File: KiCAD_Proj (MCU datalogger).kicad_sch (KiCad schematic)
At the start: 25 parts, among them U1 24LC1025-I_SM, U2 DS1337S_, U3 24LC1025-I_SM, U4 ATMEGA328P-AU, Y1 32.768 KHz, Y2 16MHz

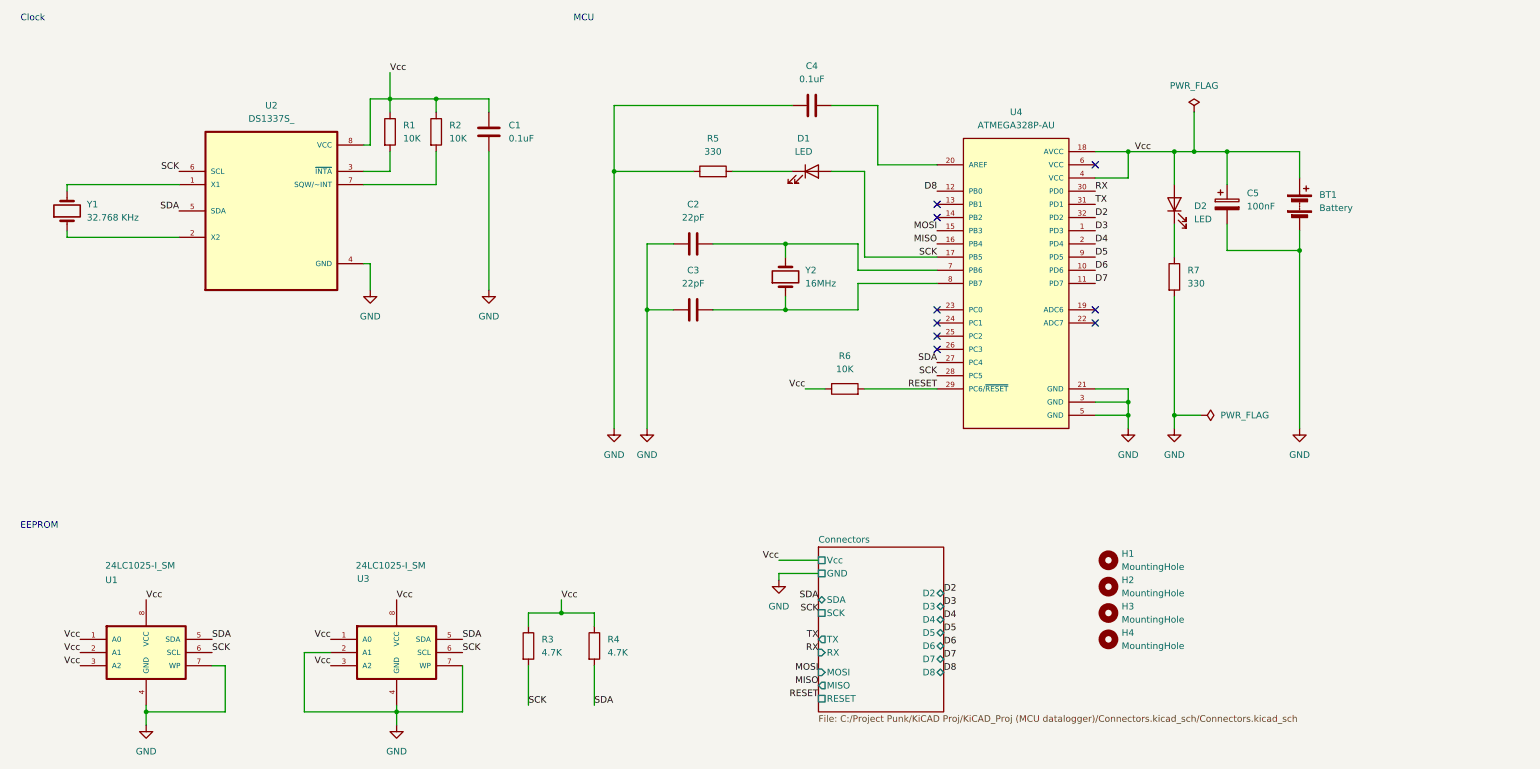
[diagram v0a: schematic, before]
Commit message: Added required symbols to schematic sheets and connectors
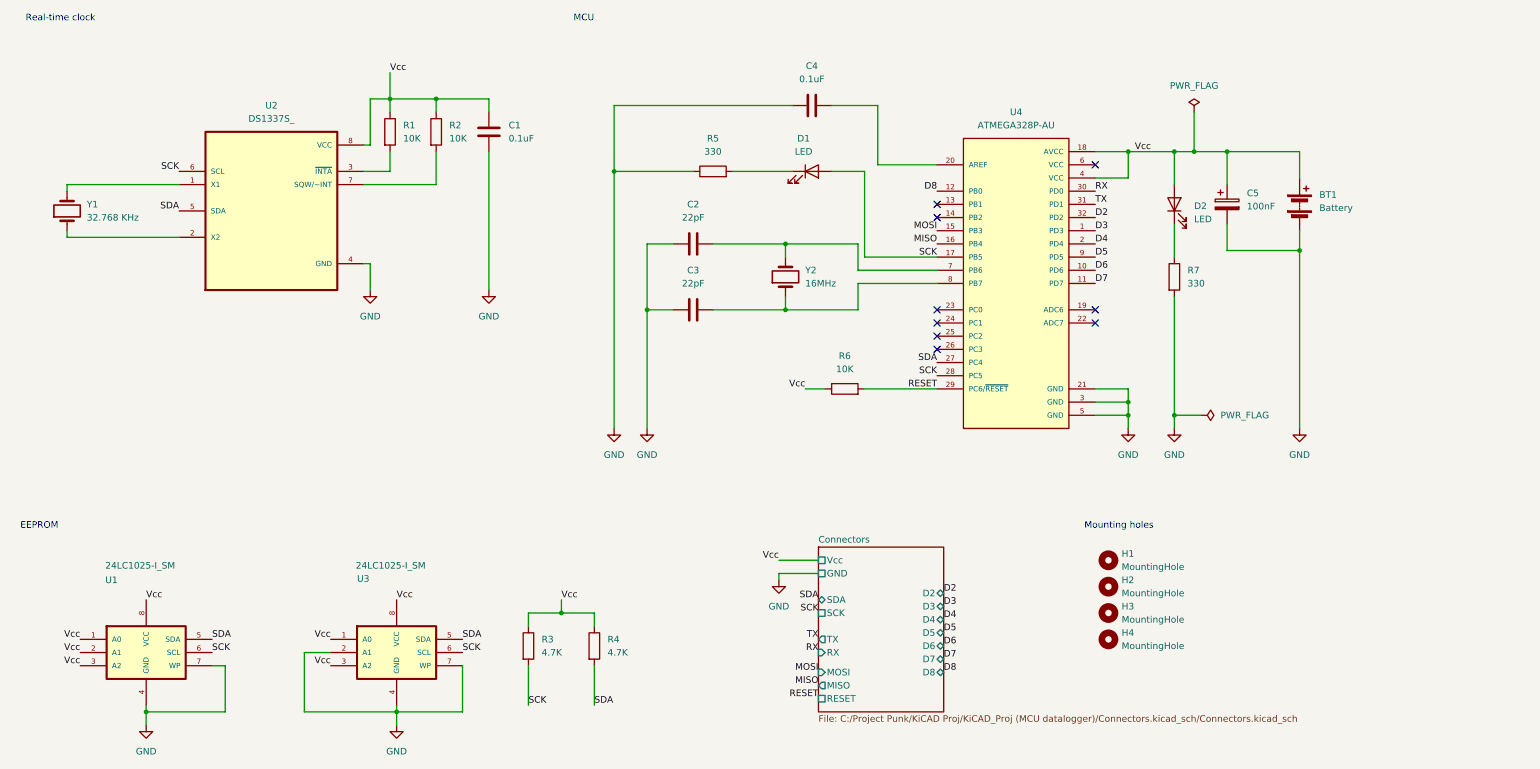
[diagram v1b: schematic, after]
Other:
- note added: "Mounting holes"
- note added: "Real-time clock"
- note removed: "Clock"
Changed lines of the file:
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@@
 		)
 	)
-	(text "Clock"
+	(text "Real-time clock"
 		(exclude_from_sim no)
-		(at 21.336 18.796 0)
+		(at 26.67 18.796 0)
+		(effects
+			(font
+				(size 1.27 1.27)
+			)
+		)
+	)
+	(text "Mounting holes"
+		(exclude_from_sim no)
+		(at 230.632 116.586 0)
 		(effects
 			(font
@@
 			)
 			(stroke
+				(width 0)
+				(type dash)
+			)
+			(fill
+				(type none)
+			)
+		)
+	)
+	(rule_area
+		(polyline
+			(pts
+				(xy 223.52 118.11) (xy 248.92 118.11) (xy 248.92 144.78) (xy 223.52 144.78)
+			)
+			(stroke

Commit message: Routing sans GND Vcc Complete.
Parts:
- C1, C2, C3, C4, C5: footprint (none) -> Capacitor_SMD:C_0805_2012Metric
- D1, D2: footprint (none) -> LED_SMD:LED_0805_2012Metric
- H1, H2, H3, H4: footprint (none) -> MountingHole:MountingHole_2.1mm
- R1, R2, R3, R4, R5, R6, R7: footprint (none) -> Resistor_SMD:R_0805_2012Metric
- Y1, Y2: footprint (none) -> Crystal:Crystal_SMD_5032-2Pin_5.0x3.2mm_HandSoldering
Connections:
- net Vcc: no longer BT1.1 (+), C5.1, D2.2 (A), U4.18 (AVCC), U4.4 (VCC)
- new net: BT1.1 (+), C5.1, D2.2 (A), U4.18 (AVCC), U4.4 (VCC)
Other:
- moved on the sheet: H1, H2, H3, H4
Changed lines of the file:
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@@
 	(text "Mounting holes"
 		(exclude_from_sim no)
-		(at 230.632 116.586 0)
+		(at 228.092 119.126 0)
 		(effects
 			(font
@@
 		)
 	)
-	(label "Vcc"
-		(at 233.68 44.45 0)
-		(effects
-			(font
-				(size 1.27 1.27)
-			)
-			(justify left bottom)
-		)
-	)
 	(label "SCK"
 		(at 116.84 151.13 0)
@@
 		(polyline
 			(pts
-				(xy 223.52 118.11) (xy 248.92 118.11) (xy 248.92 144.78) (xy 223.52 144.78)
+				(xy 220.98 120.65) (xy 246.38 120.65) (xy 246.38 147.32) (xy 220.98 147.32)
 			)
 			(stroke
@@
 	(symbol
 		(lib_id "Mechanical:MountingHole")
-		(at 228.6 133.35 0)
+		(at 226.06 135.89 0)
 		(unit 1)
 		(exclude_from_sim no)
@@
 		(fields_autoplaced yes)
 		(property "Reference" "H3"
-			(at 231.14 132.0799 0)
+			(at 228.6 134.6199 0)
 			(effects
 				(font
@@
 		)
 		(property "Value" "MountingHole"
-			(at 231.14 134.6199 0)
+			(at 228.6 137.1599 0)
 			(effects
 				(font
@@
 			)
 		)
-		(property "Footprint" ""
-			(at 228.6 133.35 0)
+		(property "Footprint" "MountingHole:MountingHole_2.1mm"
+			(at 226.06 135.89 0)
 			(effects
 				(font
@@
 		)
 		(property "Datasheet" "~"
-			(at 228.6 133.35 0)
+			(at 226.06 135.89 0)
 			(effects
 				(font
@@
 		)
 		(property "Description" "Mounting Hole without connection"
-			(at 228.6 133.35 0)
+			(at 226.06 135.89 0)
 			(effects
 				(font
@@
 	(symbol
 		(lib_id "Mechanical:MountingHole")
-		(at 228.6 138.43 0)
+		(at 226.06 140.97 0)
 		(unit 1)
 		(exclude_from_sim no)
@@
 		(fields_autoplaced yes)
 		(property "Reference" "H4"
-			(at 231.14 137.1599 0)
+			(at 228.6 139.6999 0)
 			(effects
 				(font
@@
 		)
 		(property "Value" "MountingHole"
-			(at 231.14 139.6999 0)
+			(at 228.6 142.2399 0)
 			(effects
 				(font
@@
 			)
 		)
-		(property "Footprint" ""
-			(at 228.6 138.43 0)
+		(property "Footprint" "MountingHole:MountingHole_2.1mm"
+			(at 226.06 140.97 0)
 			(effects
 				(font
@@
 		)
 		(property "Datasheet" "~"
-			(at 228.6 138.43 0)
+			(at 226.06 140.97 0)
 			(effects
 				(font
@@
 		)
 		(property "Description" "Mounting Hole without connection"
-			(at 228.6 138.43 0)
+			(at 226.06 140.97 0)
 			(effects
 				(font
@@
 			)
 		)
-		(property "Footprint" ""
+		(property "Footprint" "Capacitor_SMD:C_0805_2012Metric"
 			(at 152.4 73.9648 0)
 			(effects
@@
 			)
 		)
-		(property "Footprint" ""
+		(property "Footprint" "Capacitor_SMD:C_0805_2012Metric"
 			(at 175.26 34.5948 0)
 			(effects
@@
 	(symbol
 		(lib_id "Mechanical:MountingHole")
-		(at 228.6 128.27 0)
+		(at 226.06 130.81 0)
 		(unit 1)
 		(exclude_from_sim no)
@@
 		(fields_autoplaced yes)
 		(property "Reference" "H2"
-			(at 231.14 126.9999 0)
+			(at 228.6 129.5399 0)
 			(effects
 				(font
@@
 		)
 		(property "Value" "MountingHole"
-			(at 231.14 129.5399 0)
+			(at 228.6 132.0799 0)
 			(effects
 				(font
@@
 			)
 		)
-		(property "Footprint" ""
-			(at 228.6 128.27 0)
+		(property "Footprint" "MountingHole:MountingHole_2.1mm"
+			(at 226.06 130.81 0)
 			(effects
 				(font
@@
 		)
 		(property "Datasheet" "~"
-			(at 228.6 128.27 0)
+			(at 226.06 130.81 0)
 			(effects
 				(font
@@
 		)
 		(property "Description" "Mounting Hole without connection"
-			(at 228.6 128.27 0)
+			(at 226.06 130.81 0)
 			(effects
 				(font
@@
 	(symbol
 		(lib_id "Mechanical:MountingHole")
-		(at 228.6 123.19 0)
+		(at 226.06 125.73 0)
 		(unit 1)
 		(exclude_from_sim no)
@@
 		(fields_autoplaced yes)
 		(property "Reference" "H1"
-			(at 231.14 121.9199 0)
+			(at 228.6 124.4599 0)
 			(effects
 				(font
@@
 		)
 		(property "Value" "MountingHole"
-			(at 231.14 124.4599 0)
+			(at 228.6 126.9999 0)
 			(effects
 				(font
@@
 			)
 		)
-		(property "Footprint" ""
-			(at 228.6 123.19 0)
+		(property "Footprint" "MountingHole:MountingHole_2.1mm"
+			(at 226.06 125.73 0)
 			(effects
 				(font
@@
 		)
 		(property "Datasheet" "~"
-			(at 228.6 123.19 0)
+			(at 226.06 125.73 0)
 			(effects
 				(font
@@
 		)
 		(property "Description" "Mounting Hole without connection"
-			(at 228.6 123.19 0)
+			(at 226.06 125.73 0)
 			(effects
 				(font
@@
 			)
 		)
-		(property "Footprint" ""
+		(property "Footprint" "Resistor_SMD:R_0805_2012Metric"
 			(at 97.282 40.64 90)
 			(effects
@@
 			)
 		)
-		(property "Footprint" ""
+		(property "Footprint" "Crystal:Crystal_SMD_5032-2Pin_5.0x3.2mm_HandSoldering"
 			(at 27.94 55.88 0)
 			(effects
@@
 			)
 		)
-		(property "Footprint" ""
+		(property "Footprint" "Crystal:Crystal_SMD_5032-2Pin_5.0x3.2mm_HandSoldering"
 			(at 166.37 68.58 0)
 			(effects
@@
 			)
 		)
-		(property "Footprint" ""
+		(property "Footprint" "Resistor_SMD:R_0805_2012Metric"
 			(at 88.392 40.64 90)
 			(effects
@@
 			)
 		)
-		(property "Footprint" ""
+		(property "Footprint" "Capacitor_SMD:C_0805_2012Metric"
 			(at 110.1852 44.45 0)
 			(effects
@@
 			)
 		)
-		(property "Footprint" ""
+		(property "Footprint" "Capacitor_SMD:C_0805_2012Metric"
 			(at 252.4252 58.42 0)
 			(effects
@@
 			)
 		)
-		(property "Footprint" ""
+		(property "Footprint" "Resistor_SMD:R_0805_2012Metric"
 			(at 239.522 68.58 90)
 			(effects
@@
 			)
 		)
-		(property "Footprint" ""
+		(property "Footprint" "Resistor_SMD:R_0805_2012Metric"
 			(at 177.8 91.948 90)
 			(effects
@@
 			)
 		)
-		(property "Footprint" ""
+		(property "Footprint" "Resistor_SMD:R_0805_2012Metric"
 			(at 152.4 50.038 90)
 			(effects
@@
 			)
 		)
-		(property "Footprint" ""
+		(property "Footprint" "Resistor_SMD:R_0805_2012Metric"
 			(at 115.062 139.7 90)
 			(effects
@@
 			)
 		)
-		(property "Footprint" ""
+		(property "Footprint" "LED_SMD:LED_0805_2012Metric"
 			(at 171.45 48.26 0)
 			(effects
@@
 			)
 		)
-		(property "Footprint" ""
+		(property "Footprint" "LED_SMD:LED_0805_2012Metric"
 			(at 241.3 54.61 0)
 			(effects
@@
 			)
 		)
-		(property "Footprint" ""
+		(property "Footprint" "Resistor_SMD:R_0805_2012Metric"
 			(at 127.762 139.7 90)
 			(effects
@@
 			)
 		)
-		(property "Footprint" ""
+		(property "Footprint" "Capacitor_SMD:C_0805_2012Metric"
 			(at 152.4 61.2648 0)
 			(effects

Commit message: Fixed outstanding issues.
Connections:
- net Vcc: now also BT1.1 (+), C5.1, D2.2 (A), U4.18 (AVCC), U4.4 (VCC)
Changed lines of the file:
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@@
+		)
+	)
+	(label "Vcc"
+		(at 257.81 44.45 0)
+		(effects
+			(font
+				(size 1.27 1.27)
+			)
+			(justify left bottom)
 		)
 	)

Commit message: Finished the schematic.
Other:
- sheet Connectors: file C:/Project Punk/KiCAD Proj/KiCAD_Proj (MCU datalogger)/Connectors.kicad_sch/Connectors.kicad_sch -> C:/Project Punk/KiCAD Proj/KiCAD_Proj (MCU datalogger [4 layer])/Connectors.kicad_sch/Connectors.kicad_sch
- company: (none) -> LAUDE, RUSELLE RAE D.
- title: (none) -> MCU Datalogger
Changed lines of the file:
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@@
 	(generator_version "9.0")
 	(paper "A4")
+	(title_block
+		(title "MCU Datalogger")
+		(date "9/16/2025")
+		(company "LAUDE, RUSELLE RAE D.")
+		(comment 1 "BSECE - 1C")
+		(comment 2 "ELECTRONICS ENGINEERING DEPARTMENT")
+		(comment 3 "ELECTRONICS ENGINEERING")
+		(comment 4 "TECHNOLOGICAL UNIVERSITY OF THE PHILIPPINES")
+	)
 	(text "EEPROM"
 		(exclude_from_sim no)
@@
 	(wire
 		(pts
-			(xy 172.72 125.73) (xy 165.1 125.73)
-		)
-		(stroke
-			(width 0)
-			(type default)
-		)
-	)
-	(wire
-		(pts
 			(xy 91.44 152.4) (xy 104.14 152.4)
 		)
@@
 	(wire
 		(pts
+			(xy 165.1 123.19) (xy 172.72 123.19)
+		)
+		(stroke
+			(width 0)
+			(type default)
+		)
+	)
+	(wire
+		(pts
 			(xy 85.09 48.26) (xy 90.17 48.26)
 		)
@@
 	(wire
 		(pts
-			(xy 27.94 60.96) (xy 49.53 60.96)
+			(xy 172.72 125.73) (xy 165.1 125.73)
 		)
 		(stroke
@@
 	(wire
 		(pts
-			(xy 55.88 143.51) (xy 58.42 143.51)
+			(xy 27.94 60.96) (xy 49.53 60.96)
 		)
 		(stroke
@@
 	(wire
 		(pts
-			(xy 86.36 66.04) (xy 86.36 71.12)
+			(xy 55.88 143.51) (xy 58.42 143.51)
 		)
 		(stroke
@@
 	(wire
 		(pts
-			(xy 165.1 125.73) (xy 165.1 127)
+			(xy 86.36 66.04) (xy 86.36 71.12)
 		)
 		(stroke
@@
 	(wire
 		(pts
+			(xy 165.1 125.73) (xy 165.1 127)
+		)
+		(stroke
+			(width 0)
+			(type default)
+		)
+	)
+	(wire
+		(pts
 			(xy 129.54 135.89) (xy 129.54 133.35)
 		)
@@
 	(wire
 		(pts
-			(xy 165.1 123.19) (xy 172.72 123.19)
-		)
-		(stroke
-			(width 0)
-			(type default)
-		)
-	)
-	(wire
-		(pts
 			(xy 241.3 95.25) (xy 241.3 97.79)
 		)
@@
 			)
 		)
-		(property "Sheetfile" "C:/Project Punk/KiCAD Proj/KiCAD_Proj (MCU datalogger)/Connectors.kicad_sch/Connectors.kicad_sch"
+		(property "Sheetfile" "C:/Project Punk/KiCAD Proj/KiCAD_Proj (MCU datalogger [4 layer])/Connectors.kicad_sch/Connectors.kicad_sch"
 			(at 172.72 152.9846 0)
 			(effects
@@
 			)
 		)
-		(pin "Vcc" passive
-			(at 172.72 123.19 180)
+		(pin "D2" tri_state
+			(at 196.85 129.54 0)
 			(effects
 				(font
 					(size 1.27 1.27)
 				)
-				(justify left)
+				(justify right)
 			)
 		)
-		(pin "GND" passive
-			(at 172.72 125.73 180)
+		(pin "D3" tri_state
+			(at 196.85 132.08 0)
 			(effects
 				(font
 					(size 1.27 1.27)
 				)
-				(justify left)
+				(justify right)
 			)
 		)
-		(pin "SDA" tri_state
-			(at 172.72 130.81 180)
+		(pin "D4" tri_state
+			(at 196.85 134.62 0)
 			(effects
 				(font
 					(size 1.27 1.27)
 				)
-				(justify left)
+				(justify right)
 			)
 		)
-		(pin "SCK" passive
-			(at 172.72 133.35 180)
+		(pin "D5" tri_state
+			(at 196.85 137.16 0)
 			(effects
 				(font
 					(size 1.27 1.27)
 				)
-				(justify left)
+				(justify right)
 			)
 		)
-		(pin "TX" output
-			(at 172.72 138.43 180)
+		(pin "D6" tri_state
+			(at 196.85 139.7 0)
 			(effects
 				(font
 					(size 1.27 1.27)
 				)
-				(justify left)
+				(justify right)
 			)
 		)
-		(pin "RX" input
-			(at 172.72 140.97 180)
+		(pin "D7" tri_state
+			(at 196.85 142.24 0)
 			(effects
 				(font
 					(size 1.27 1.27)
 				)
-				(justify left)
+				(justify right)
 			)
 		)
-		(pin "MOSI" input
-			(at 172.72 144.78 180)
+		(pin "D8" tri_state
+			(at 196.85 144.78 0)
 			(effects
 				(font
 					(size 1.27 1.27)
 				)
-				(justify left)
+				(justify right)
 			)
 		)
-		(pin "MISO" output
-			(at 172.72 147.32 180)
+		(pin "GND" passive
+			(at 172.72 125.73 180)
 			(effects
 				(font
@@
 			)
 		)
-		(pin "RESET" passive
-			(at 172.72 149.86 180)
+		(pin "Vcc" passive
+			(at 172.72 123.19 180)
 			(effects
 				(font
@@
 			)
 		)
-		(pin "D2" tri_state
-			(at 196.85 129.54 0)
+		(pin "MISO" output
+			(at 172.72 147.32 180)
 			(effects
 				(font
 					(size 1.27 1.27)
 				)
-				(justify right)
+				(justify left)
 			)
 		)
-		(pin "D3" tri_state
-			(at 196.85 132.08 0)
+		(pin "MOSI" input
+			(at 172.72 144.78 180)
 			(effects
 				(font
 					(size 1.27 1.27)
 				)
-				(justify right)
+				(justify left)
 			)
 		)
-		(pin "D4" tri_state
-			(at 196.85 134.62 0)
+		(pin "RESET" passive
+			(at 172.72 149.86 180)
 			(effects
 				(font
 					(size 1.27 1.27)
 				)
-				(justify right)
+				(justify left)
 			)
 		)
-		(pin "D5" tri_state
-			(at 196.85 137.16 0)
+		(pin "RX" input
+			(at 172.72 140.97 180)
 			(effects
 				(font
 					(size 1.27 1.27)
 				)
-				(justify right)
+				(justify left)
 			)
 		)
-		(pin "D6" tri_state
-			(at 196.85 139.7 0)
+		(pin "TX" output
+			(at 172.72 138.43 180)
 			(effects
 				(font
 					(size 1.27 1.27)
 				)
-				(justify right)
+				(justify left)
 			)
 		)
-		(pin "D7" tri_state
-			(at 196.85 142.24 0)
+		(pin "SDA" tri_state
+			(at 172.72 130.81 180)
 			(effects
 				(font
 					(size 1.27 1.27)
 				)
-				(justify right)
+				(justify left)
 			)
 		)
-		(pin "D8" tri_state
-			(at 196.85 144.78 0)
+		(pin "SCK" passive
+			(at 172.72 133.35 180)
 			(effects
 				(font
 					(size 1.27 1.27)
 				)
-				(justify right)
+				(justify left)
 			)
 		)
@@
 			(project "KiCAD_Proj (MCU datalogger)"
 				(path "/4bd39814-648a-43e5-9d59-9775154104be"
-					(page "2")
+					(page "3")
 				)
 			)

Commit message: Fixed bugs in schematic.
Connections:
- net SCK: no longer R3.2, U1.6 (SCL), U2.6 (SCL), U3.6 (SCL), U4.28 (PC5)
- new net SCL: R3.2, U1.6 (SCL), U2.6 (SCL), U3.6 (SCL), U4.28 (PC5)
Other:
- sheet Connectors ports: added SCL; removed none
